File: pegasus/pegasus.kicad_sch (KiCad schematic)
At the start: 14 parts, among them IC1 RFD900, IC2 Adafruit_MPL3115A2, IC3 Adafruit-BNO055-PCB, IC4 L70B-M39, IC5 L7805ACV, J1 Conn_01x02_Female, J2 Conn_01x02_Female, U1 Teensy4.1, U2 CON-SMA-EDGE-S, U3 CON-SMA-EDGE-S

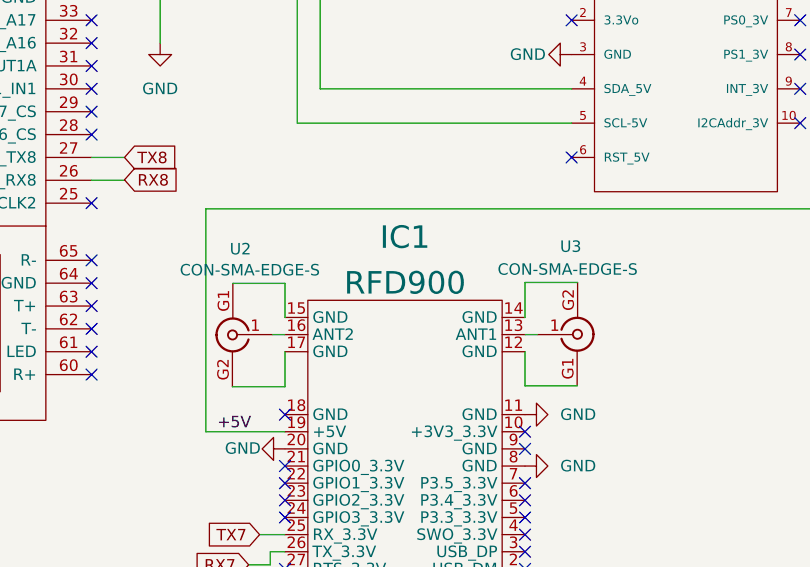
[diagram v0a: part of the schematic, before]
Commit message: removed adafruit sensors from RFD900 library
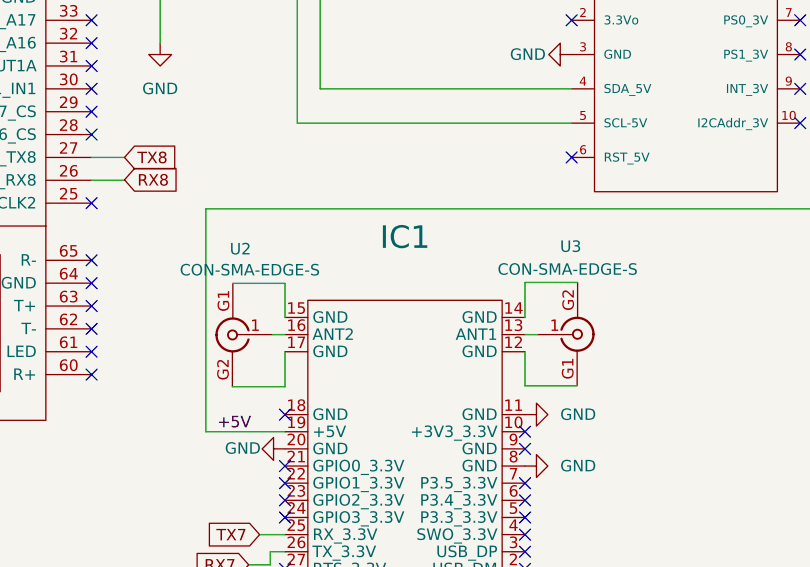
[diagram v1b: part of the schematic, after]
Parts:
- IC1: value RFD900 -> (none)
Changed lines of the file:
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@@
       (effects (font (size 2.5 2.5)))
     )
-    (property "Value" "RFD900" (id 1) (at 132.6134 158.75 0)
+    (property "Value" "" (id 1) (at 132.6134 158.75 0)
       (effects (font (size 2.5 2.5)))
     )
